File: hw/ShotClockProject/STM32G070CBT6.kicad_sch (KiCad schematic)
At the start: 28 parts, among them J1 Conn_01x06_Pin, J2 Conn_ST_STDC14, SW1 SW_SPDT, U1 STM32G070CBTx, U2 LD39015M33R, Y1 16MHz

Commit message: Finished routing and added silk + part nmbr
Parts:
- C10, C11: LCSC Part # C107007 -> (none)
- C4, C9: LCSC Part # C1525 -> (none)
- C5: LCSC Part # C96446 -> (none)
- C6: LCSC Part # C15195 -> (none)
- C7, C8, C9: LCSC Part # C52923 -> (none)
- C9: LCSC Part C52923 -> C1525; LCSC Part # C52923 -> (none)
- D1: LCSC Part # C264451 -> (none)
- FB1: LCSC Part # C127301 -> (none)
- J1: LCSC Part # C56816 -> (none)
- J2: LCSC Part # C3975190 -> (none)
- R1, R32: LCSC Part # C25744 -> (none)
- R2: LCSC Part # C25867 -> (none)
- R2: LCSC Part # C25076 -> (none)
- R2: LCSC Part # C477610 -> (none)
- SW1: LCSC Part # C500057 -> (none)
- U2: LCSC Part # C2798212 -> (none)
- Y1: LCSC Part # C112972 -> (none)
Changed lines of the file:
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@@
       (effects (font (size 1.27 1.27)) hide)
     )
-    (property "LCSC Part #" "C25867" (at 196.85 86.36 0)
+    (property "LCSC Part #" "" (at 196.85 86.36 0)
       (effects (font (size 1.27 1.27)) hide)
     )
@@
       (effects (font (size 1.27 1.27)) hide)
     )
-    (property "LCSC Part #" "C2798212" (at 69.85 129.54 0)
+    (property "LCSC Part #" "" (at 69.85 129.54 0)
       (effects (font (size 1.27 1.27)) hide)
     )
@@
       (effects (font (size 1.27 1.27)) hide)
     )
-    (property "LCSC Part #" "C56816" (at 269.875 86.995 0)
+    (property "LCSC Part #" "" (at 269.875 86.995 0)
       (effects (font (size 1.27 1.27)) hide)
     )
@@
       (effects (font (size 1.27 1.27)) hide)
     )
-    (property "LCSC Part #" "C52923" (at 51.435 130.81 0)
-      (effects (font (size 1.27 1.27)) hide)
-    )
-    (property "LCSC Part" "C52923" (at 51.435 130.81 0)
+    (property "LCSC Part #" "" (at 51.435 130.81 0)
+      (effects (font (size 1.27 1.27)) hide)
+    )
+    (property "LCSC Part" "C1525" (at 51.435 130.81 0)
       (effects (font (size 1.27 1.27)) hide)
     )
@@
       (effects (font (size 1.27 1.27)) hide)
     )
-    (property "LCSC Part #" "C107007" (at 55.88 91.44 0)
+    (property "LCSC Part #" "" (at 55.88 91.44 0)
       (effects (font (size 1.27 1.27)) hide)
     )
@@
       (effects (font (size 1.27 1.27)) hide)
     )
-    (property "LCSC Part #" "C52923" (at 92.075 130.81 0)
+    (property "LCSC Part #" "" (at 92.075 130.81 0)
       (effects (font (size 1.27 1.27)) hide)
     )
@@
       (effects (font (size 1.27 1.27)) hide)
     )
-    (property "LCSC Part #" "C25076" (at 264.16 150.495 0)
+    (property "LCSC Part #" "" (at 264.16 150.495 0)
       (effects (font (size 1.27 1.27)) hide)
     )
@@
       (effects (font (size 1.27 1.27)) hide)
     )
-    (property "LCSC Part #" "C52923" (at 81.28 130.81 0)
-      (effects (font (size 1.27 1.27)) hide)
-    )
-    (property "LCSC Part" "C52923" (at 81.28 130.81 0)
+    (property "LCSC Part #" "" (at 81.28 130.81 0)
+      (effects (font (size 1.27 1.27)) hide)
+    )
+    (property "LCSC Part" "C1525" (at 81.28 130.81 0)
       (effects (font (size 1.27 1.27)) hide)
     )
@@
       (effects (font (size 1.27 1.27)) hide)
     )
-    (property "LCSC Part #" "C1525" (at 49.53 60.96 0)
+    (property "LCSC Part #" "" (at 49.53 60.96 0)
       (effects (font (size 1.27 1.27)) hide)
     )
@@
       (effects (font (size 1.27 1.27)) hide)
     )
-    (property "LCSC Part #" "C3975190" (at 261.62 127.635 0)
+    (property "LCSC Part #" "" (at 261.62 127.635 0)
       (effects (font (size 1.27 1.27)) hide)
     )
@@
       (effects (font (size 1.27 1.27)) hide)
     )
-    (property "LCSC Part #" "C15195" (at 226.06 41.91 0)
+    (property "LCSC Part #" "" (at 226.06 41.91 0)
       (effects (font (size 1.27 1.27)) hide)
     )
@@
       (effects (font (size 1.27 1.27)) hide)
     )
-    (property "LCSC Part #" "C25744" (at 212.725 145.415 0)
+    (property "LCSC Part #" "" (at 212.725 145.415 0)
       (effects (font (size 1.27 1.27)) hide)
     )
@@
       (effects (font (size 1.27 1.27)) hide)
     )
-    (property "LCSC Part #" "C477610" (at 177.8 133.35 0)
+    (property "LCSC Part #" "" (at 177.8 133.35 0)
       (effects (font (size 1.27 1.27)) hide)
     )
@@
       (effects (font (size 1.27 1.27)) hide)
     )
-    (property "LCSC Part #" "C264451" (at 167.64 133.35 0)
+    (property "LCSC Part #" "" (at 167.64 133.35 0)
       (effects (font (size 1.27 1.27)) hide)
     )
@@
       (effects (font (size 1.27 1.27)) hide)
     )
-    (property "LCSC Part #" "C25744" (at 236.22 133.985 0)
+    (property "LCSC Part #" "" (at 236.22 133.985 0)
       (effects (font (size 1.27 1.27)) hide)
     )
@@
       (effects (font (size 1.27 1.27)) hide)
     )
-    (property "LCSC Part #" "C112972" (at 43.18 82.55 0)
+    (property "LCSC Part #" "" (at 43.18 82.55 0)
       (effects (font (size 1.27 1.27)) hide)
     )
@@
       (effects (font (size 1.27 1.27)) hide)
     )
-    (property "LCSC Part #" "C52923" (at 41.275 130.81 0)
+    (property "LCSC Part #" "" (at 41.275 130.81 0)
       (effects (font (size 1.27 1.27)) hide)
     )
@@
       (effects (font (size 1.27 1.27)) hide)
     )
-    (property "LCSC Part #" "C25867" (at 196.85 71.755 0)
+    (property "LCSC Part #" "" (at 196.85 71.755 0)
       (effects (font (size 1.27 1.27)) hide)
     )
@@
       (effects (font (size 1.27 1.27)) hide)
     )
-    (property "LCSC Part #" "C52923" (at 262.89 41.91 0)
+    (property "LCSC Part #" "" (at 262.89 41.91 0)
       (effects (font (size 1.27 1.27)) hide)
     )
@@
       (effects (font (size 1.27 1.27)) hide)
     )
-    (property "LCSC Part #" "C52923" (at 238.76 41.91 0)
+    (property "LCSC Part #" "" (at 238.76 41.91 0)
       (effects (font (size 1.27 1.27)) hide)
     )
@@
       (effects (font (size 1.27 1.27)) hide)
     )
-    (property "LCSC Part #" "C1525" (at 111.76 43.18 0)
+    (property "LCSC Part #" "" (at 111.76 43.18 0)
       (effects (font (size 1.27 1.27)) hide)
     )
@@
       (effects (font (size 1.27 1.27)) hide)
     )
-    (property "LCSC Part #" "C127301" (at 251.46 38.1 0)
+    (property "LCSC Part #" "" (at 251.46 38.1 0)
       (effects (font (size 1.27 1.27)) hide)
     )
@@
       (effects (font (size 1.27 1.27)) hide)
     )
-    (property "LCSC Part #" "C96446" (at 97.79 43.18 0)
+    (property "LCSC Part #" "" (at 97.79 43.18 0)
       (effects (font (size 1.27 1.27)) hide)
     )
@@
       (effects (font (size 1.27 1.27)) hide)
     )
-    (property "LCSC Part #" "C25744" (at 250.19 85.725 0)
+    (property "LCSC Part #" "" (at 250.19 85.725 0)
       (effects (font (size 1.27 1.27)) hide)
     )
@@
       (effects (font (size 1.27 1.27)) hide)
     )
-    (property "LCSC Part #" "C107007" (at 31.75 91.44 0)
+    (property "LCSC Part #" "" (at 31.75 91.44 0)
       (effects (font (size 1.27 1.27)) hide)
     )
@@
       (effects (font (size 1.27 1.27)) hide)
     )
-    (property "LCSC Part #" "C500057" (at 198.755 145.415 0)
-      (effects (font (size 1.27 1.27)) hide)
-    )
+    (property "LCSC Part #" "" (at 198.755 145.415 0)
+      (effects (font (size 1.27 1.27)) hide)
+    )

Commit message: Updated part NBRS for mainboard
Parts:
- C10, C11: LCSC Part C107007 -> C1575
- C5: value 4700n -> 4.7u; LCSC Part C96446 -> C23733
- R2: value 130R -> 100R; LCSC Part C477610 -> C25076
- U1: LCSC Part (none) -> C529338
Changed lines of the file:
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@@
-      (effects (font (size 1.27 1.27)) hide)
-    )
-    (property "LCSC Part #" "" (at 196.85 86.36 0)
       (effects (font (size 1.27 1.27)) hide)
     )
@@
     )
     (property "Datasheet" "http://www.st.com/resource/en/datasheet/ld39015.pdf" (at 69.85 129.54 0)
-      (effects (font (size 1.27 1.27)) hide)
-    )
-    (property "LCSC Part #" "" (at 69.85 129.54 0)
       (effects (font (size 1.27 1.27)) hide)
     )
@@
     )
     (property "Datasheet" "~" (at 269.875 86.995 0)
-      (effects (font (size 1.27 1.27)) hide)
-    )
-    (property "LCSC Part #" "" (at 269.875 86.995 0)
       (effects (font (size 1.27 1.27)) hide)
     )
@@
       (effects (font (size 1.27 1.27)) hide)
     )
-    (property "LCSC Part #" "" (at 51.435 130.81 0)
-      (effects (font (size 1.27 1.27)) hide)
-    )
     (property "LCSC Part" "C1525" (at 51.435 130.81 0)
       (effects (font (size 1.27 1.27)) hide)
@@
       (effects (font (size 1.27 1.27)) hide)
     )
-    (property "LCSC Part #" "" (at 130.81 46.99 0)
-      (effects (font (size 1.27 1.27)) hide)
-    )
     (property "LCSC Part" "" (at 130.81 46.99 0)
       (effects (font (size 1.27 1.27)) hide)
@@
       (effects (font (size 1.27 1.27)) hide)
     )
-    (property "LCSC Part #" "" (at 55.88 91.44 0)
-      (effects (font (size 1.27 1.27)) hide)
-    )
-    (property "LCSC Part" "C107007" (at 55.88 91.44 0)
+    (property "LCSC Part" "C1575" (at 55.88 91.44 0)
       (effects (font (size 1.27 1.27)) hide)
     )
@@
       (effects (font (size 1.27 1.27)) hide)
     )
-    (property "LCSC Part #" "" (at 92.075 130.81 0)
-      (effects (font (size 1.27 1.27)) hide)
-    )
     (property "LCSC Part" "C52923" (at 92.075 130.81 0)
       (effects (font (size 1.27 1.27)) hide)
@@
       (effects (font (size 1.27 1.27)) hide)
     )
-    (property "LCSC Part #" "" (at 264.16 150.495 0)
-      (effects (font (size 1.27 1.27)) hide)
-    )
     (property "LCSC Part" "C25076" (at 264.16 150.495 0)
       (effects (font (size 1.27 1.27)) hide)
@@
       (effects (font (size 1.27 1.27)) hide)
     )
-    (property "LCSC Part #" "" (at 81.28 130.81 0)
-      (effects (font (size 1.27 1.27)) hide)
-    )
     (property "LCSC Part" "C1525" (at 81.28 130.81 0)
       (effects (font (size 1.27 1.27)) hide)
@@
     )
     (property "Datasheet" "~" (at 49.53 60.96 0)
-      (effects (font (size 1.27 1.27)) hide)
-    )
-    (property "LCSC Part #" "" (at 49.53 60.96 0)
       (effects (font (size 1.27 1.27)) hide)
     )
@@
     )
     (property "Datasheet" "https://www.st.com/content/ccc/resource/technical/document/user_manual/group1/99/49/91/b6/b2/3a/46/e5/DM00526767/files/DM00526767.pdf/jcr:content/translations/en.DM00526767.pdf" (at 270.51 159.385 90)
-      (effects (font (size 1.27 1.27)) hide)
-    )
-    (property "LCSC Part #" "" (at 261.62 127.635 0)
       (effects (font (size 1.27 1.27)) hide)
     )
@@
       (effects (font (size 1.27 1.27)) hide)
     )
-    (property "LCSC Part #" "" (at 226.06 41.91 0)
-      (effects (font (size 1.27 1.27)) hide)
-    )
     (property "LCSC Part" "C15195" (at 226.06 41.91 0)
       (effects (font (size 1.27 1.27)) hide)
@@
       (effects (font (size 1.27 1.27)) hide)
     )
-    (property "LCSC Part #" "" (at 212.725 145.415 0)
-      (effects (font (size 1.27 1.27)) hide)
-    )
     (property "LCSC Part" "C25744" (at 212.725 145.415 0)
       (effects (font (size 1.27 1.27)) hide)
@@
       (effects (font (size 1.27 1.27)) (justify left))
     )
-    (property "Value" "130R" (at 176.53 139.7 0)
+    (property "Value" "100R" (at 176.53 139.7 0)
       (effects (font (size 1.27 1.27)) (justify left))
     )
@@
       (effects (font (size 1.27 1.27)) hide)
     )
-    (property "LCSC Part #" "" (at 177.8 133.35 0)
-      (effects (font (size 1.27 1.27)) hide)
-    )
-    (property "LCSC Part" "C477610" (at 177.8 133.35 0)
+    (property "LCSC Part" "C25076" (at 177.8 133.35 0)
       (effects (font (size 1.27 1.27)) hide)
     )
@@
       (effects (font (size 1.27 1.27)) hide)
     )
-    (property "LCSC Part #" "" (at 167.64 133.35 0)
-      (effects (font (size 1.27 1.27)) hide)
-    )
     (property "LCSC Part" "C264451" (at 167.64 133.35 0)
       (effects (font (size 1.27 1.27)) hide)
@@
     )
     (property "Datasheet" "~" (at 236.22 133.985 0)
-      (effects (font (size 1.27 1.27)) hide)
-    )
-    (property "LCSC Part #" "" (at 236.22 133.985 0)
       (effects (font (size 1.27 1.27)) hide)
     )
@@
       (effects (font (size 1.27 1.27)) hide)
     )
-    (property "LCSC Part #" "" (at 43.18 82.55 0)
-      (effects (font (size 1.27 1.27)) hide)
-    )
     (property "LCSC Part" "C112972" (at 43.18 82.55 0)
       (effects (font (size 1.27 1.27)) hide)
@@
       (effects (font (size 1.27 1.27)) hide)
     )
-    (property "LCSC Part #" "" (at 41.275 130.81 0)
-      (effects (font (size 1.27 1.27)) hide)
-    )
     (property "LCSC Part" "C52923" (at 41.275 130.81 0)
       (effects (font (size 1.27 1.27)) hide)
@@
       (effects (font (size 1.27 1.27)) hide)
     )
-    (property "LCSC Part #" "" (at 196.85 71.755 0)
-      (effects (font (size 1.27 1.27)) hide)
-    )
     (property "LCSC Part" "C25867" (at 196.85 71.755 0)
       (effects (font (size 1.27 1.27)) hide)
@@
     )
     (property "Datasheet" "~" (at 262.89 41.91 0)
-      (effects (font (size 1.27 1.27)) hide)
-    )
-    (property "LCSC Part #" "" (at 262.89 41.91 0)
       (effects (font (size 1.27 1.27)) hide)
     )
@@
     )
     (property "Datasheet" "https://www.st.com/resource/en/datasheet/stm32g070cb.pdf" (at 128.27 100.33 0)
+      (effects (font (size 1.27 1.27)) hide)
+    )
+    (property "LCSC Part" "C529338" (at 128.27 100.33 0)
       (effects (font (size 1.27 1.27)) hide)
     )
@@
       (effects (font (size 1.27 1.27)) hide)
     )
-    (property "LCSC Part #" "" (at 238.76 41.91 0)
-      (effects (font (size 1.27 1.27)) hide)
-    )
     (property "LCSC Part" "C52923" (at 238.76 41.91 0)
       (effects (font (size 1.27 1.27)) hide)
@@
       (effects (font (size 1.27 1.27)) hide)
     )
-    (property "LCSC Part #" "" (at 111.76 43.18 0)
-      (effects (font (size 1.27 1.27)) hide)
-    )
     (property "LCSC Part" "C1525" (at 111.76 43.18 0)
       (effects (font (size 1.27 1.27)) hide)
@@
       (effects (font (size 1.27 1.27)) hide)
     )
-    (property "LCSC Part #" "" (at 251.46 38.1 0)
-      (effects (font (size 1.27 1.27)) hide)
-    )
     (property "LCSC Part" "C127301" (at 251.46 38.1 0)
       (effects (font (size 1.27 1.27)) hide)
@@
       (effects (font (size 1.27 1.27)) (justify left))
     )
-    (property "Value" "4700n" (at 100.965 44.45 0)
+    (property "Value" "4.7u" (at 100.965 44.45 0)
       (effects (font (size 1.27 1.27)) (justify left))
     )
@@
       (effects (font (size 1.27 1.27)) hide)
     )
-    (property "LCSC Part #" "" (at 97.79 43.18 0)
-      (effects (font (size 1.27 1.27)) hide)
-    )
-    (property "LCSC Part" "C96446" (at 97.79 43.18 0)
+    (property "LCSC Part" "C23733" (at 97.79 43.18 0)
       (effects (font (size 1.27 1.27)) hide)
     )
@@
     )
     (property "Datasheet" "~" (at 250.19 85.725 0)
-      (effects (font (size 1.27 1.27)) hide)
-    )
-    (property "LCSC Part #" "" (at 250.19 85.725 0)
       (effects (font (size 1.27 1.27)) hide)
     )
@@
       (effects (font (size 1.27 1.27)) hide)
     )
-    (property "LCSC Part #" "" (at 31.75 91.44 0)
-      (effects (font (size 1.27 1.27)) hide)
-    )
-    (property "LCSC Part" "C107007" (at 31.75 91.44 0)
+    (property "LCSC Part" "C1575" (at 31.75 91.44 0)
       (effects (font (size 1.27 1.27)) hide)
     )
@@
       (effects (font (size 1.27 1.27)) hide)
     )
-    (property "LCSC Part #" "" (at 198.755 145.415 0)
-      (effects (font (size 1.27 1.27)) hide)
-    )

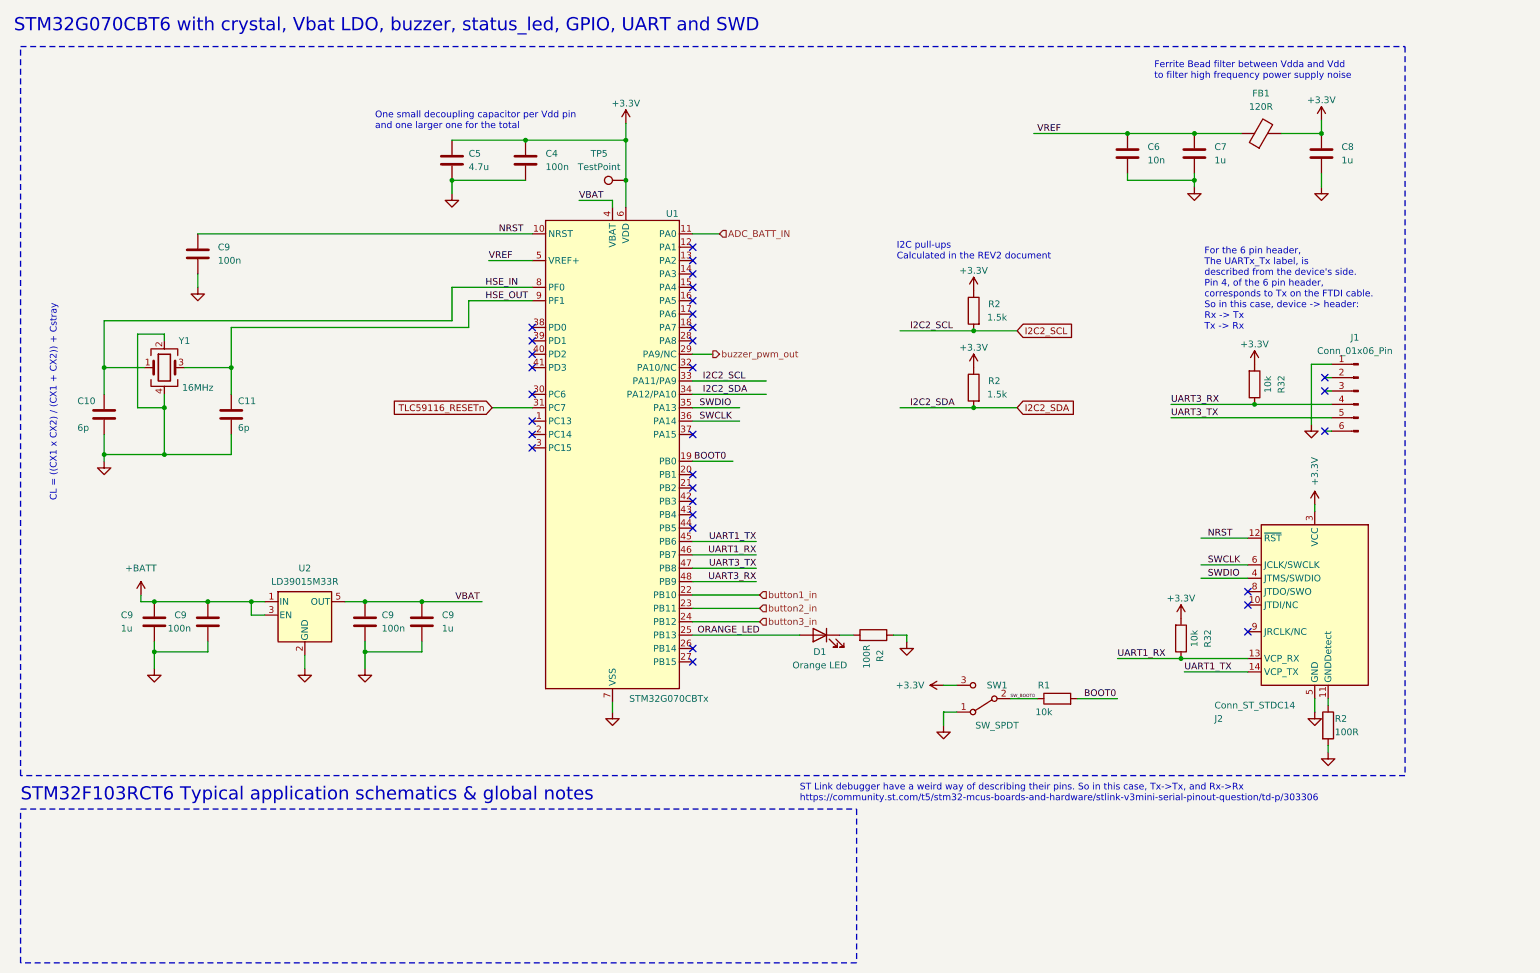
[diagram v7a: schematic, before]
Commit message: Add REV3 odt file, update CubeMX version and fix the ADC readout for battery voltage.
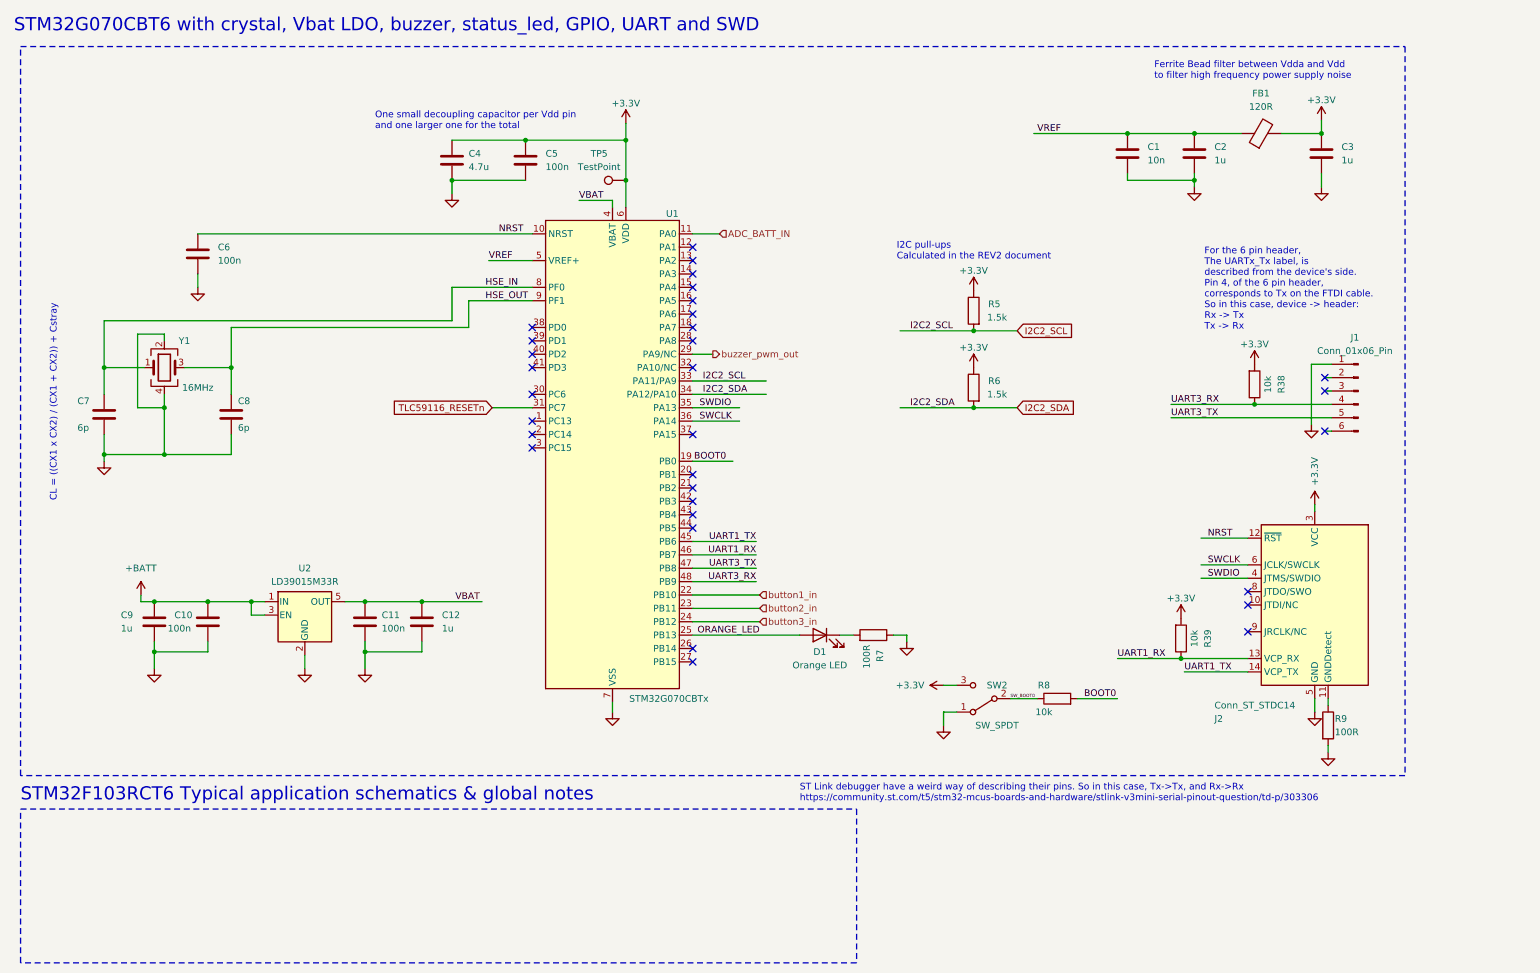
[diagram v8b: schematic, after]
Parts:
- renumbered C6 to C1, C9 to C10, C9 to C11, C9 to C12, C7 to C2, C8 to C3, C5 to C4, C4 to C5, C9 to C6, C10 to C7, C11 to C8, R32 to R38, R32 to R39, R2 to R5, R2 to R6, R2 to R7, R1 to R8, R2 to R9, SW1 to SW2
